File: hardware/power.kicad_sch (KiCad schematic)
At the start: 61 parts, among them IC1 LMR38020FDDAR, Q1 LMR51635XDDCR, Q2 LMR51635XDDCR, T1 TP_VCC, T10 TP_+3V3, T11 TP_+5V, T12 TP_+5V, T2 TP_VCC, T3 TP_VCC, T4 TP_VCC, T5 TP_+6V6S1, T6 TP_+6V6S1, T7 TP_+6V6S2, T8 TP_+6V6S2, U2 LM1117-3.3

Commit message: schematic & pcb update
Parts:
- removed C20: 10u, Capacitor_SMD:C_0603_1608Metric_Pad1.08x0.95mm_HandSolder, symbol Device:C_Small
- removed C23: 100n, Capacitor_SMD:C_0603_1608Metric_Pad1.08x0.95mm_HandSolder, symbol Device:C_Small
- removed C29: 47u, Capacitor_SMD:C_0603_1608Metric_Pad1.08x0.95mm_HandSolder, symbol Device:C_Small
- removed D2: +5V, LED_SMD:LED_0603_1608Metric, symbol Device:LED_Small
- removed IC1: LMR38020FDDAR, Package_SO:SOIC-8-1EP_3.9x4.9mm_P1.27mm_EP2.29x3mm, symbol SamacSys_Parts:LMR38020FDDAR
- removed L3: 15u/2A, SamacSys_Parts:VLS6045, symbol Device:L_Small
- removed R10: 10k, Resistor_SMD:R_0603_1608Metric_Pad0.98x0.95mm_HandSolder, symbol Device:R_Small
- removed R7: 64k9, Resistor_SMD:R_0603_1608Metric_Pad0.98x0.95mm_HandSolder, symbol Device:R_Small
- removed R8: 1k, Resistor_SMD:R_0603_1608Metric_Pad0.98x0.95mm_HandSolder, symbol Device:R_Small
- removed R9: 40k2, Resistor_SMD:R_0603_1608Metric_Pad0.98x0.95mm_HandSolder, symbol Device:R_Small
- added C24, C28, C31: 22u, Capacitor_SMD:C_0805_2012Metric, symbol Device:C_Small
- added C25: 100n, Capacitor_SMD:C_0603_1608Metric, symbol Device:C_Small
- added D4: 600W/28V, Diode_SMD:D_SOD-323_HandSoldering, symbol Diode:SD24_SOD323
- added D5: 9V1, Diode_SMD:D_SOD-323_HandSoldering, symbol Device:D_Zener_Small
- added IC1: TPS54202HDDCR, Package_TO_SOT_SMD:SOT-23-6, symbol SamacsysNew:TPS54202HDDCR
- added L3: 68u/1A4, Inductor_SMD:L_TDK_VLS6045EX_VLS6045AF, symbol Samacsys_kicad_sym:SRR4028-271Y
- added Q1: SI2347DS-T1-GE3, Package_TO_SOT_SMD:SOT-23_Handsoldering, symbol Simulation_SPICE:PMOS
- added R11: 510k, Resistor_SMD:R_0603_1608Metric, symbol Device:R_Small
- added R12: 13k3, Resistor_SMD:R_0603_1608Metric, symbol Device:R_Small
- added R13: 100k, Resistor_SMD:R_0603_1608Metric, symbol Device:R_Small
- added R6: 100k, Resistor_SMD:R_0603_1608Metric_Pad0.98x0.95mm_HandSolder, symbol Device:R_Small
- C26, C27: Mouser Price/Stock https://www.mouser.pl/ProductDetail/KEMET/C0603C104J5RACTM?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 -> https://www.mouser.pl/datasheet/2/447/KEM_C1002_X7R_SMD-331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
- C30: value 47u -> 22u; footprint Capacitor_SMD:C_0603_1608Metric_Pad1.08x0.95mm_HandSolder -> Capacitor_SMD:C_0805_2012Metric; Manufacturer_Name (none) -> MCASH21GCC7684MTCA1J; Manufacturer_Part_Number (none) -> CL21A107MQYNNWE; Mouser Part Number (none) -> 810-C2012X5R1V226MAC; Mouser Price/Stock https://www.mouser.pl/ProductDetail/Murata-Electronics/GRM3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 -> (none)
- D7: renamed from D3; Mouser Price/Stock https://www.we-online.com/components/products/datasheet/150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 -> https://www.mouser.pl/ProductDetail/Wurth-Elektronik/150060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
- renumbered C12 to C10, C13 to C11, C15 to C12, C16 to C13, C6 to C14, C9 to C15, C14 to C16, C21 to C20, C22 to C21, C24 to C22, C25 to C23, C28 to C29, C7 to C6, C8 to C7, C10 to C8, C11 to C9, D1 to D6, Q1 to Q2, Q2 to Q3, R6 to R10, R11 to R14, R3 to R7, R4 to R8, R5 to R9, T2 to T1, T12 to T10, T10 to T11, T3 to T2, T1 to T3, T5 to T4, T6 to T5, T7 to T6, T8 to T7, T4 to T8, T11 to T9, TP9 to TP1
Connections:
- net BOOT_+5V: now also IC1.6 (BOOT)
- net FB_+5V: now also IC1.4 (FB), R12.2, R13.1
- net GND: now also C24.2, C25.1, C28.2, C31.2, D4.1 (A1), IC1.1 (GND), R12.1, R6.2
- net SW_+5V: now also IC1.2 (SW), L3.1
- net VCC: now also C14.1, C15.1, C16.1, C17.1, C24.1, C25.2, D5.1 (K), IC1.3 (VIN), Q1.3 (S), R11.2
- net D2_to_R14 renamed D3V3_to_R1k
- net FUSE_+5V renamed +5V_OUT
- net +5V_OUT: now also C28.1, C31.1, L3.2, R13.2
- removed net VCC_IN: C14.1, C15.1, C16.1, C17.1, F1.2, T3.1
- new net EN: IC1.5 (EN), R11.1
- new net RPP_D: D4.2 (A2), F1.2, Q1.1 (D), T3.1
- new net RPP_G: D5.2 (A), Q1.2 (G), R6.1
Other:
- note added: "POWER VCC RPP & DECOUPLING"
- note added: "RPP"
- note removed: "POWER VCC DECOUPLING"
- moved on the sheet: C14, C15, C16, C17, C26, C29, D6, D7, F1, F4, F5, R14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

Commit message: schematic & pcb udpate
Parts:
- F5: footprint SamacSys_Parts:MINIASMDC260F162 -> Fuse:Fuse_1812_4532Metric_Pad1.30x3.40mm_HandSolder
- L2: footprint SamacSys_Parts:VLS6045 -> Inductor_SMD:L_TDK_VLS6045EX_VLS6045AF
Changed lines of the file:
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@@
 			)
 		)
-		(property "Footprint" "SamacSys_Parts:VLS6045"
+		(property "Footprint" "Inductor_SMD:L_TDK_VLS6045EX_VLS6045AF"
 			(at 107.95 167.64 0)
 			(effects
@@
 		(dnp no)
 		(property "Reference" "D4"
-			(at 39.624 61.976 90)
+			(at 30.48 60.96 90)
 			(effects
 				(font
@@
 		)
 		(property "Value" "600W/28V"
-			(at 32.512 56.388 0)
+			(at 33.02 63.5 90)
 			(effects
 				(font
@@
 			)
 		)
-		(property "Footprint" "SamacSys_Parts:MINIASMDC260F162"
+		(property "Footprint" "Fuse:Fuse_1812_4532Metric_Pad1.30x3.40mm_HandSolder"
 			(at 245.11 52.07 0)
 			(effects

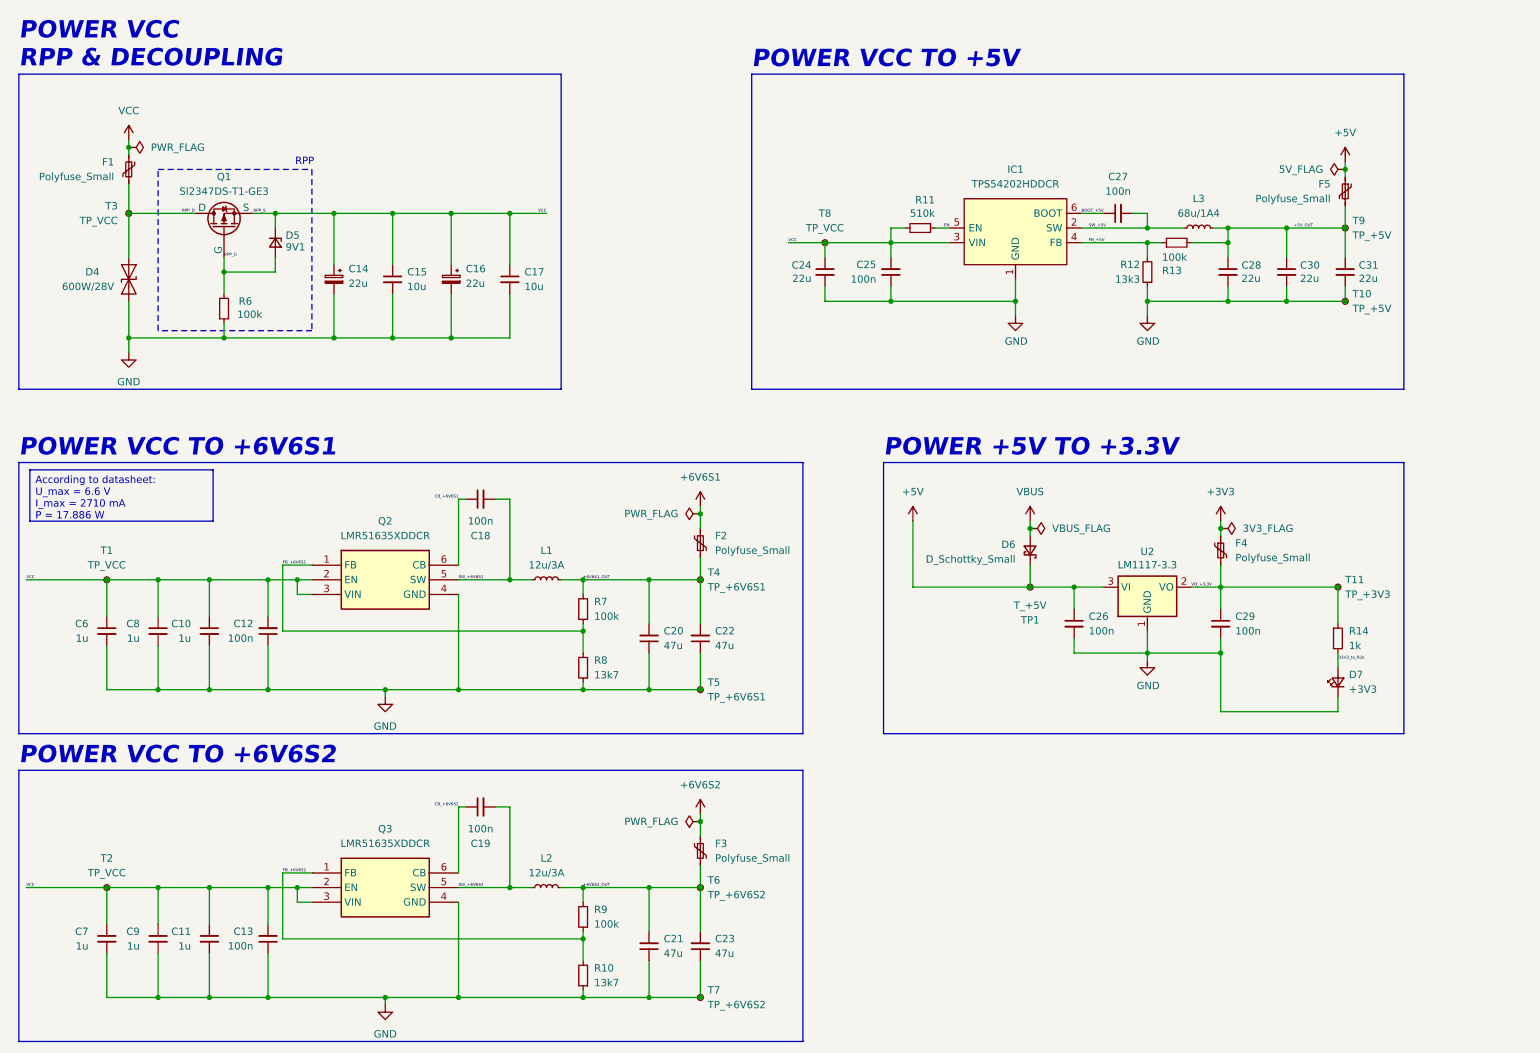
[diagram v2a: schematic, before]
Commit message: usbc changed, foots for electro cap and +5 lay
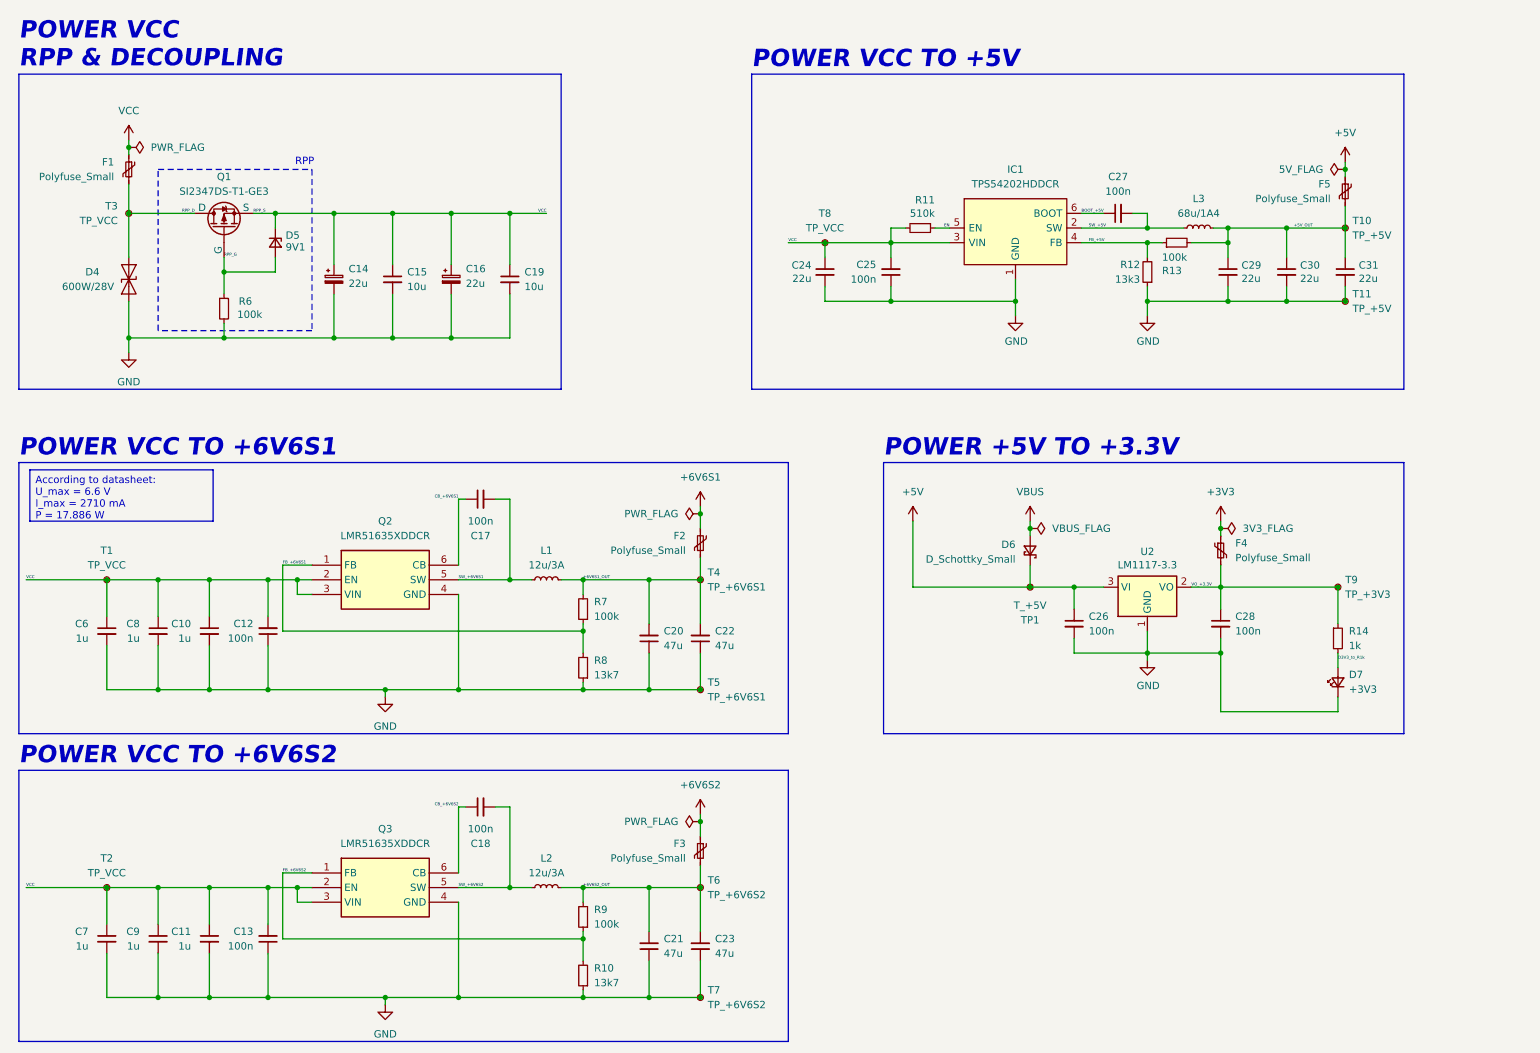
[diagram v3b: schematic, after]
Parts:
- C14, C16: footprint SamacSys_Parts:CAPPM7343X310N -> Capacitor_SMD:CP_Elec_4x5.8; Mouser Part Number 647-UCM1V220MCL1GS -> (none); Mouser Price/Stock https://www.mouser.pl/ProductDetail/TDK/C2012X5R1V226M125AC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 -> https://www.mouser.pl/ProductDetail/Nichicon/UCM1V220MCL1GS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
- C24, C30, C31: footprint Capacitor_SMD:C_0805_2012Metric -> Capacitor_SMD:C_0805_2012Metric_Pad1.18x1.45mm_HandSolder; Mouser Price/Stock (none) -> https://www.mouser.pl/ProductDetail/TDK/C2012X5R1V226M125AC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
- C25: footprint Capacitor_SMD:C_0603_1608Metric -> Capacitor_SMD:C_0603_1608Metric_Pad1.08x0.95mm_HandSolder; Mouser Price/Stock https://www.mouser.pl/ProductDetail/KEMET/C0603C104J3RACTU?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 -> https://www.mouser.pl/ProductDetail/KEMET/C0603C104J5RACTM?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
- C26, C27: Mouser Price/Stock https://www.mouser.pl/datasheet/2/447/KEM_C1002_X7R_SMD-331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 -> https://www.mouser.pl/ProductDetail/KEMET/C0603C104J5RACTM?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
- C29: renamed from C28; footprint Capacitor_SMD:C_0805_2012Metric -> Capacitor_SMD:C_0805_2012Metric_Pad1.18x1.45mm_HandSolder; Mouser Price/Stock (none) -> https://www.mouser.pl/ProductDetail/TDK/C2012X5R1V226M125AC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
- F4, F5: footprint Fuse:Fuse_1812_4532Metric_Pad1.30x3.40mm_HandSolder -> Fuse:Fuse_0805_2012Metric_Pad1.15x1.40mm_HandSolder; Mouser Price/Stock https://www.mouser.pl/ProductDetail/Littelfuse/MINIASMDC260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 -> https://www.mouser.pl/ProductDetail/Littelfuse/PICOSMDC050S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
- Q3: footprint SamacSys_Parts:SOT95P280X110-6N -> Package_TO_SOT_SMD:SOT-23-6_Handsoldering
- R13: footprint Resistor_SMD:R_0603_1608Metric -> Resistor_SMD:R_0603_1608Metric_Pad0.98x0.95mm_HandSolder; Mouser Price/Stock https://www.mouser.pl/ProductDetail/YAGEO/RT0603DRE07100KL?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 -> https://www.mouser.pl/ProductDetail/KOA-Speer/RK73B1JTTD104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
- R6: Mouser Price/Stock (none) -> https://www.mouser.pl/ProductDetail/KOA-Speer/RK73B1JTTD104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
- renumbered C18 to C17, C19 to C18, C17 to C19, C29 to C28, T9 to T10, T10 to T11, T11 to T9
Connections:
- net +6V6S1: now also F2.2; no longer F2.1
- net +6V6S1_OUT: now also F2.1; no longer F2.2

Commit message: pcb & footprint update
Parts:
- C10, C11, C6, C7, C8, C9: Mouser Price/Stock https://www.mouser.pl/ProductDetail/TAIYO-YUDEN/MMJCG168CB7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 -> https://www.mouser.pl/ProductDetail/Murata-Electronics/GRT1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
- C12, C13, C17, C18, C25, C26, C27, C28: Mouser Price/Stock https://www.mouser.pl/ProductDetail/KEMET/C0603C104J5RACTM?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 -> https://www.mouser.pl/ProductDetail/Murata-Electronics/GRM0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
- C20, C21, C22, C23: footprint Capacitor_SMD:C_0603_1608Metric_Pad1.08x0.95mm_HandSolder -> Capacitor_SMD:C_0805_2012Metric_Pad1.18x1.45mm_HandSolder; Mouser Price/Stock https://www.mouser.pl/ProductDetail/Murata-Electronics/GRM3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 -> https://www.mouser.pl/ProductDetail/Murata-Electronics/GRM2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
- D4: footprint Diode_SMD:D_SOD-323_HandSoldering -> Diode_SMD:D_SMB_Handsoldering
- D6: footprint Diode_SMD:D_SOD-123 -> Diode_SMD:D_SOD-123F
- D7: footprint LED_SMD:LED_0603_1608Metric -> LED_SMD:LED_0603_1608Metric_Pad1.05x0.95mm_HandSolder
- F1: footprint Fuse:Fuse_1206_3216Metric_Pad1.42x1.75mm_HandSolder -> Fuse:Fuse_0805_2012Metric_Pad1.15x1.40mm_HandSolder; Mouser Price/Stock https://www.mouser.pl/ProductDetail/Bourns/SF-1206HH800R-2?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 -> https://www.mouser.pl/ProductDetail/Vishay-Beyschlag/MFU080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
- F2, F3: Mouser Price/Stock https://www.mouser.pl/ProductDetail/Eaton-Electronics/PTSLR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 -> https://www.mouser.pl/ProductDetail/Littelfuse/0805L400SLWR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
- IC1: footprint Package_TO_SOT_SMD:SOT-23-6 -> Package_TO_SOT_SMD:SOT-23-6_Handsoldering
- R11, R12: footprint Resistor_SMD:R_0603_1608Metric -> Resistor_SMD:R_0603_1608Metric_Pad0.98x0.95mm_HandSolder
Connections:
- net RPP_D is gone; now on net RPP_G: D4.2 (A2), F1.2, Q1.1 (D), T3.1
- net RPP_G: no longer D5.2 (A), Q1.2 (G), R6.1
- new net RPP_S: D5.2 (A), Q1.2 (G), R6.1

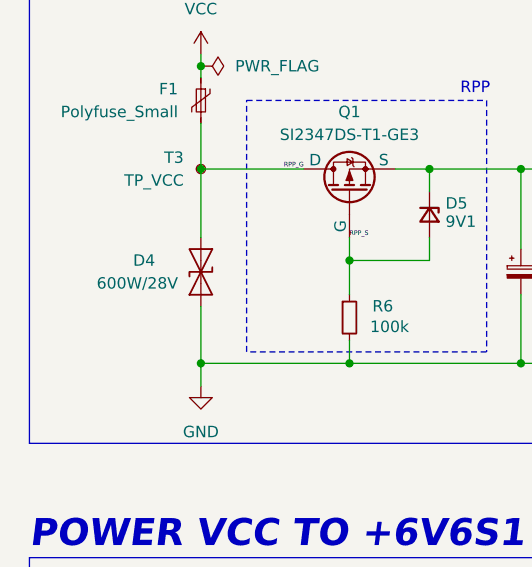
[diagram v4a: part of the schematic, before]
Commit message: d4 - footprint change
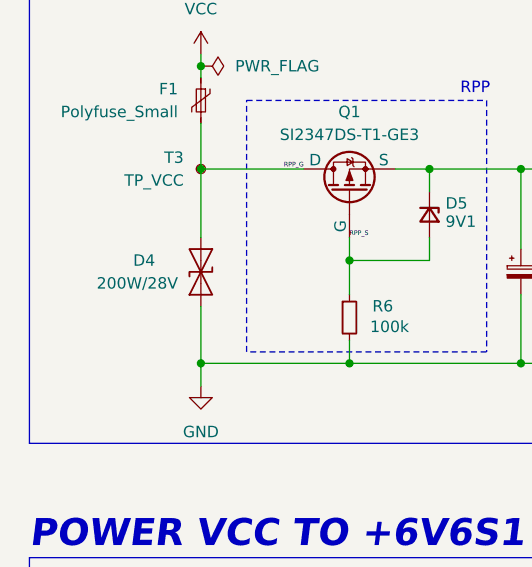
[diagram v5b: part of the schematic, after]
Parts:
- D4: value 600W/28V -> 200W/28V; footprint Diode_SMD:D_SMB_Handsoldering -> Diode_SMD:D_SOD-123; Mouser Price/Stock https://www.mouser.pl/ProductDetail/Diodes-Incorporated/SMB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 -> https://www.mouser.pl/ProductDetail/Littelfuse/SMF28CA?qs=d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
- Q1: footprint Package_TO_SOT_SMD:SOT-23_Handsoldering -> Package_TO_SOT_SMD:SOT-23-3
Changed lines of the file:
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@@
 			)
 		)
-		(property "Footprint" "Package_TO_SOT_SMD:SOT-23_Handsoldering"
+		(property "Footprint" "Package_TO_SOT_SMD:SOT-23-3"
 			(at 49.53 48.26 0)
 			(effects
@@
 			)
 		)
-		(property "Sim.Pins" "1=D 2=G 3=S"
+		(property "Sim.Pins" "1=G 2=S 3=D"
 			(at 67.31 53.34 0)
 			(effects
@@
 			)
 		)
-		(property "Value" "600W/28V"
+		(property "Value" "200W/28V"
 			(at 33.02 63.5 90)
 			(effects
@@
 			)
 		)
-		(property "Footprint" "Diode_SMD:D_SMB_Handsoldering"
+		(property "Footprint" "Diode_SMD:D_SOD-123"
 			(at 30.48 62.23 0)
 			(effects
@@
 			)
 		)
-		(property "Datasheet" "https://www.mouser.pl/datasheet/2/115/DIOD_S_A0003133144_1-2542279.pdf"
+		(property "Datasheet" "https://www.littelfuse.com/assetdocs/tvs-diodes-smf-datasheet?assetguid=7EB8A5B6-BDD0-4561-8F19-0C3CC6F9B2AF"
 			(at 35.56 62.23 0)
 			(effects
@@
 			)
 		)
-		(property "Mouser Price/Stock" "https://www.mouser.pl/ProductDetail/Diodes-Incorporated/SMBJ28CA-13-F?qs=gaDBXWSqsDDXWCpMWf3eLg%3D%3D&utm_id=9882661914&utm_source=google&utm_medium=cpc&utm_marketing_tactic=emeacorp&gad_source=1&gclid=CjwKCAiAn9a9BhBtEiwAbKg6fh0V29tkkuyN0gQZGeXOM6ynNZMM7chC9yELf7HuXjdvcz6TrNcCIxoC9psQAvD_BwE"
+		(property "Mouser Price/Stock" "https://www.mouser.pl/ProductDetail/Littelfuse/SMF28CA?qs=d0WKAl%2BL4KYaAuaKHnfQCA%3D%3D"
 			(at 35.56 62.23 0)
 			(effects
